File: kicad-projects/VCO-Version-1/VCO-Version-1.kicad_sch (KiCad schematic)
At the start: 41 parts

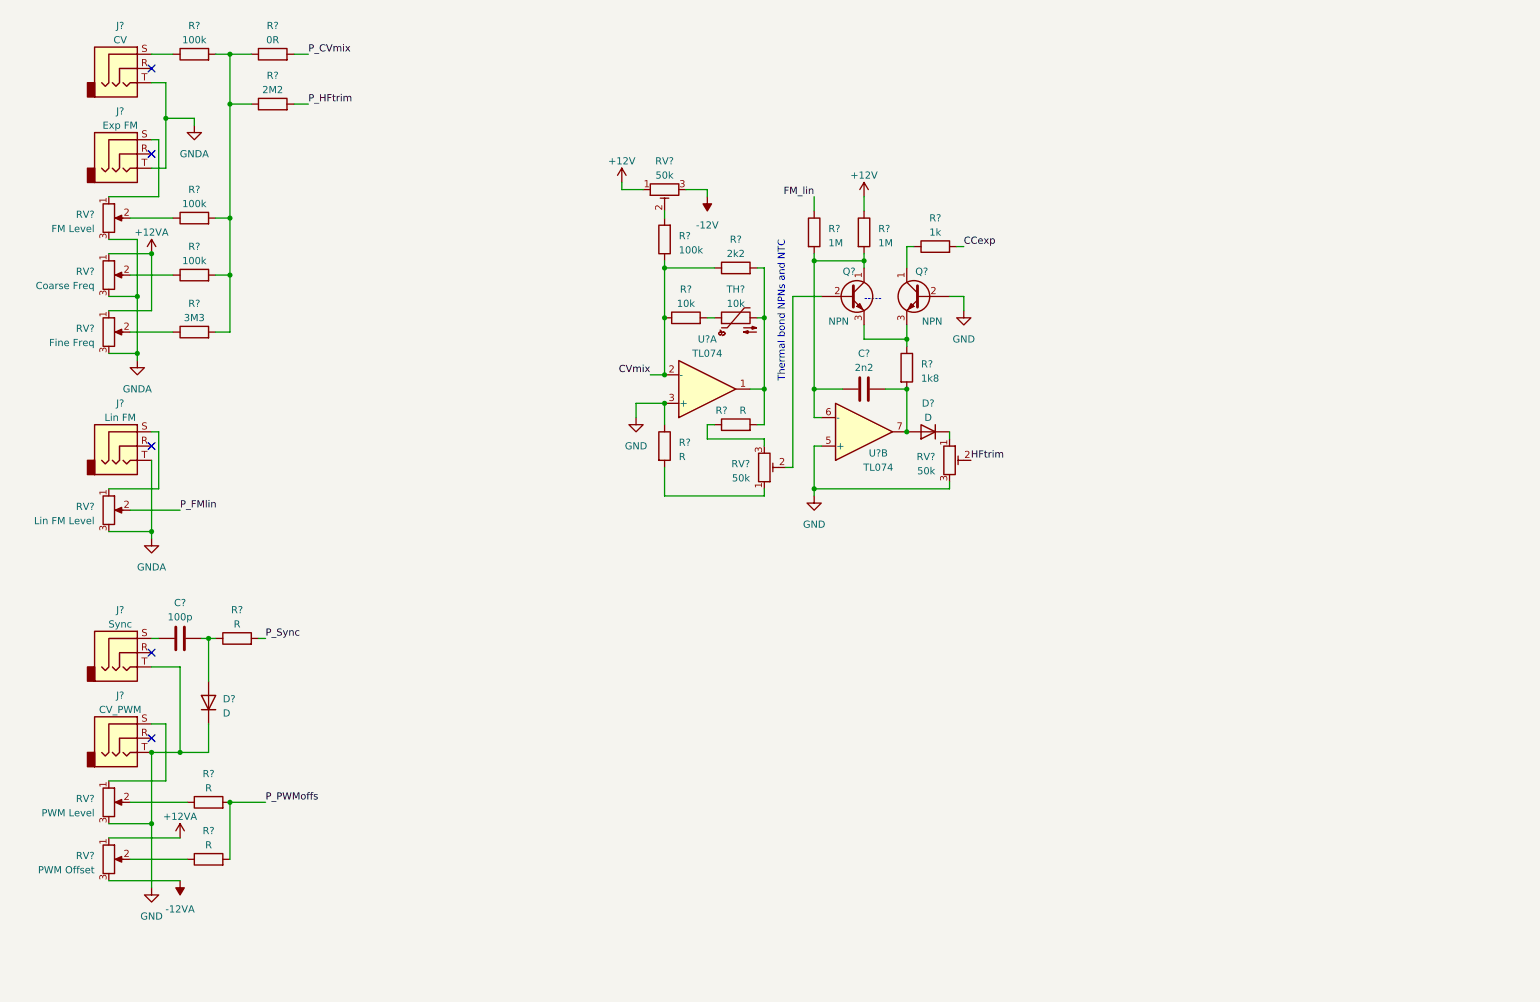
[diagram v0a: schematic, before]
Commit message: Completed schematic for VCO-1
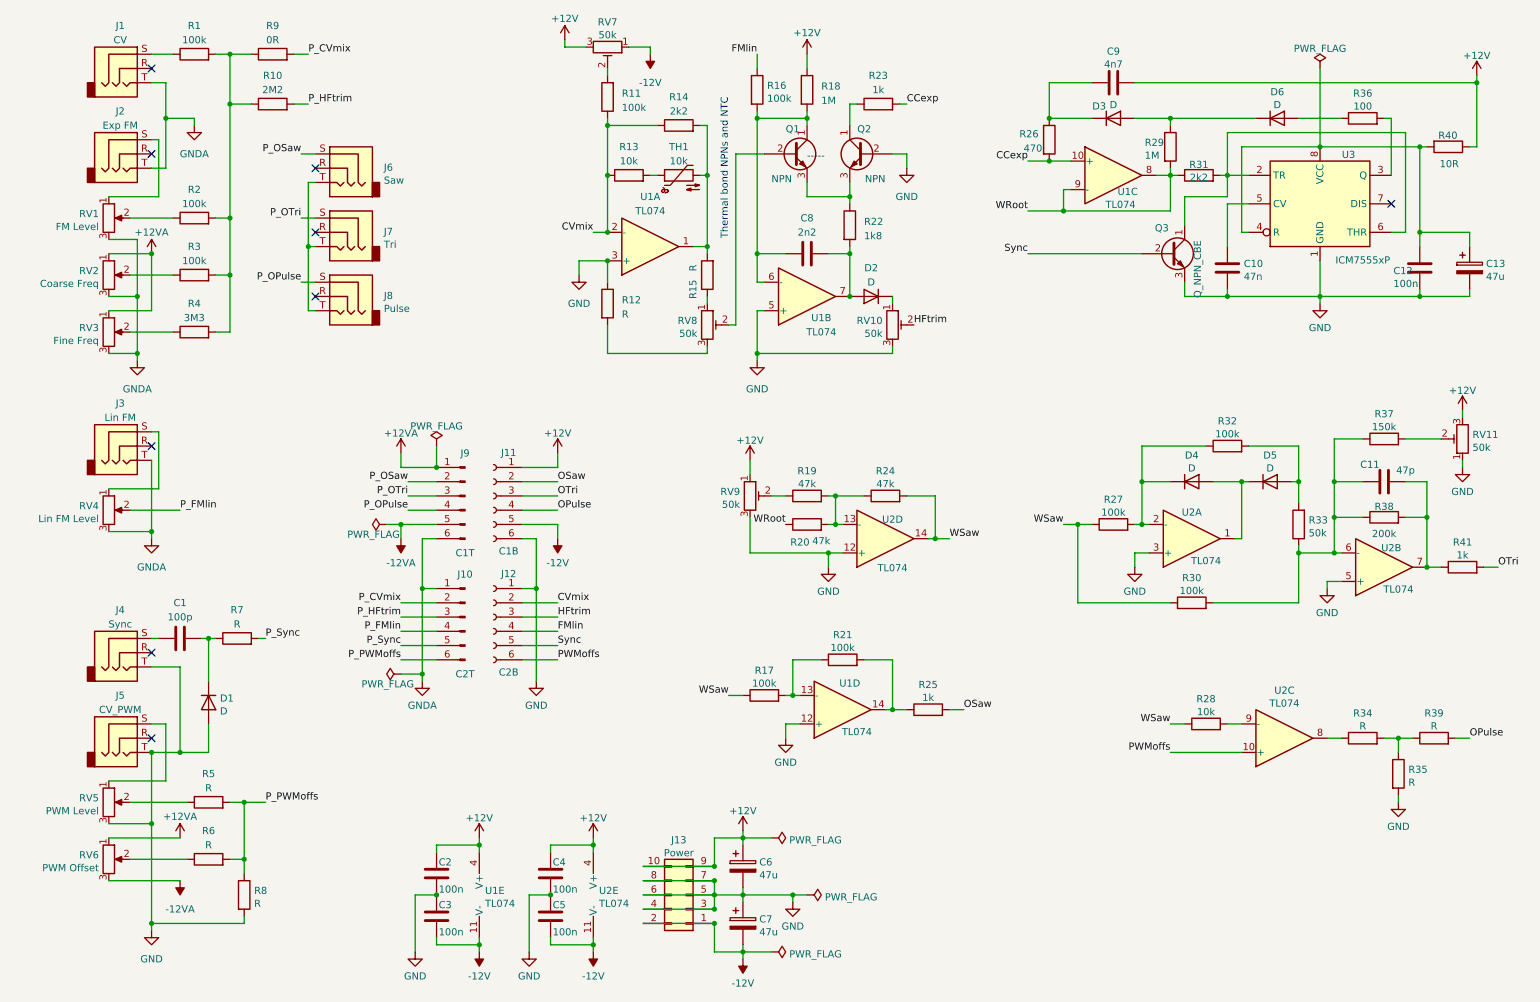
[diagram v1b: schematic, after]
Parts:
- removed RV?: FM Level, symbol Device:R_Potentiometer
- removed RV?: Lin FM Level, symbol Device:R_Potentiometer
- removed RV? (x3): 50k, symbol Device:R_Potentiometer_Trim
- removed RV?: PWM Offset, symbol Device:R_Potentiometer
- removed RV?: Fine Freq, symbol Device:R_Potentiometer
- removed RV?: Coarse Freq, symbol Device:R_Potentiometer
- removed RV?: PWM Level, symbol Device:R_Potentiometer
- added C10: 47n, symbol Device:C
- added C11: 47p, symbol Device:C
- added C12, C2, C3, C4, C5: 100n, symbol Device:C
- added C13, C6, C7: 47u, symbol Device:CP
- added C9: 4n7, symbol Device:C
- added D3, D4, D5, D6: D, symbol Device:D
- added J10: C2T, symbol Connector:Conn_01x06_Male
- added J11: C1B, symbol Connector:Conn_01x06_Female
- added J12: C2B, symbol Connector:Conn_01x06_Female
- added J13: Power, symbol Connector_Generic:Conn_02x05_Odd_Even
- added J6: Saw, symbol Connector:AudioJack3
- added J7: Tri, symbol Connector:AudioJack3
- added J8: Pulse, symbol Connector:AudioJack3
- added J9: C1T, symbol Connector:Conn_01x06_Male
- added Q3: Q_NPN_CBE, symbol Device:Q_NPN_CBE
- added R17, R21, R27, R30, R32: 100k, symbol Device:R
- added R19, R20, R24: 47k, symbol Device:R
- added R25, R41: 1k, symbol Device:R
- added R26: 470, symbol Device:R
- added R28: 10k, symbol Device:R
- added R29: 1M, symbol Device:R
- added R31: 2k2, symbol Device:R
- added R33: 50k, symbol Device:R
- added R34, R35, R39, R8: R, symbol Device:R
- added R36: 100, symbol Device:R
- added R37: 150k, symbol Device:R
- added R38: 200k, symbol Device:R
- added R40: 10R, symbol Device:R
- added RV1: FM Level, symbol Device:R_POT
- added RV10, RV11, RV7, RV8, RV9: 50k, symbol Device:R_POT_TRIM
- added RV2: Coarse Freq, symbol Device:R_POT
- added RV3: Fine Freq, symbol Device:R_POT
- added RV4: Lin FM Level, symbol Device:R_POT
- added RV5: PWM Level, symbol Device:R_POT
- added RV6: PWM Offset, symbol Device:R_POT
- added unit 3 of U1
- added unit 5 of U1
- added unit 4 of U1
- added U2: TL074, symbol Amplifier_Operational:TL074
- added U3: ICM7555xP, Package_DIP:DIP-8_W7.62mm, symbol Timer:ICM7555xP
- R16: renamed from R?; value 1M -> 100k
- gave numbers to parts that had none: 30
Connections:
- net +12V: now also C2.1, C4.1, C6.1, C9.2, J11.1 (Pin_1), J13.10 (Pin_10), J13.9 (Pin_9), R40.1, RV11.3, RV7.3, RV9.1, U1.4 (V+), U2.4 (V+)
- net +12VA: now also J9.1 (Pin_1), RV2.1, RV3.1, RV6.1
- net -12V: now also C3.2, C5.2, C7.2, J11.5 (Pin_5), J13.1 (Pin_1), J13.2 (Pin_2), RV7.1, U1.11 (V-), U2.11 (V-)
- net -12VA: now also J9.5 (Pin_5), RV6.3
- net CCexp: now also R26.2, U1.10 (+)
- net CVmix: now also J12.2 (Pin_2)
- net GND: now also D1.2 (A), C10.2, C12.2, C13.2, C2.2, C3.1, C4.2, C5.1, C6.2, C7.1, J11.6 (Pin_6), J12.1 (Pin_1), J13.3 (Pin_3), J13.4 (Pin_4), J13.5 (Pin_5), J13.6 (Pin_6), J13.7 (Pin_7), J13.8 (Pin_8), Q3.3 (E), R35.2, R8.2, RV10.3, RV11.1, RV5.3, RV9.3, U1.12 (+), U2.12 (+), U2.3 (+), U2.5 (+), U3.1 (GND); no longer D1.1 (K)
- net GNDA: now also J10.1 (Pin_1), J9.6 (Pin_6), RV1.3, RV2.3, RV3.3, RV4.3
- net HFtrim: now also J12.3 (Pin_3), RV10.2
- net P_CVmix: now also J10.2 (Pin_2)
- net P_FMlin: now also J10.4 (Pin_4), RV4.2
- net P_HFtrim: now also J10.3 (Pin_3)
- net P_PWMoffs: now also J10.6 (Pin_6), R8.1
- net P_Sync: now also J10.5 (Pin_5)
- net at J2.S: now also RV1.1
- net at R2.1: now also RV1.2
- net at R12.2: now also RV8.3
- net at Q1.2 (B): now also RV8.2
- net at J5.S: now also RV5.1
- net at J3.S: now also RV4.1
- net at R15.1: now also RV8.1
- net at R6.1: now also RV6.2
- net at C1.2, R7.1: now also D1.1 (K); no longer D1.2 (A)
- net at D2.1 (K): now also RV10.1
- net at R3.1: now also RV2.2
- net at R4.1: now also RV3.2
- net at R11.2: now also RV7.2
- net at R5.1: now also RV5.2
- net FM_lin renamed FMlin
- net FMlin: now also J12.4 (Pin_4)
- new net: C11.1, R30.2, R33.1, R37.1, R38.1, U2.6 (-)
- new net: C11.2, R38.2, R41.1, U2.7
- new net: R28.2, U2.9 (-)
- new net: R19.2, R20.2, R24.1, U2.13 (-)
- new net: D4.2 (A), D5.1 (K), U2.1
- new net: D4.1 (K), R27.2, R32.1, U2.2 (-)
- new net: C9.1, D3.1 (K), R26.1
- new net: C10.1, U3.5 (CV)
- new net: C12.1, C13.1, R40.2, U3.4 (R), U3.8 (VCC)
- new net: R34.2, R35.1, R39.1
- new net: R19.1, RV9.2
- new net: R17.2, R21.1, U1.13 (-)
- new net: Q3.1 (C), R31.2, U3.2 (TR), U3.6 (THR)
- new net: R36.2, U3.3 (Q)
- new net: J6.T, J7.T, J8.T
- new net: R34.1, U2.8
- new net: D5.2 (A), R32.2, R33.2
- new net: D3.2 (A), D6.1 (K), R29.1
- new net: D6.2 (A), R36.1
- new net: R21.2, R25.1, U1.14
- new net: R37.2, RV11.2
- new net OPulse: J11.4 (Pin_4), R39.2
- new net OSaw: J11.2 (Pin_2), R25.2
- new net OTri: J11.3 (Pin_3), R41.2
- new net PWMoffs: J12.6 (Pin_6), U2.10 (+)
- new net P_OPulse: J8.S, J9.4 (Pin_4)
- new net P_OSaw: J6.S, J9.2 (Pin_2)
- new net P_OTri: J7.S, J9.3 (Pin_3)
- new net Sync: J12.5 (Pin_5), Q3.2 (B)
- new net WRoot: R20.1, R29.2, R31.1, U1.8, U1.9 (-)
- new net WSaw: R17.1, R24.2, R27.1, R28.1, R30.1, U2.14
- no-connect marks 5 -> 9
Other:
- title: 40106 based VCO -> Three Wave VCO - v1
- moved on the sheet: C8, D1, D2, Q1, Q2, R11, R12, R13, R14, R15, R16, R18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

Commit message: Worked more on VCO1 PCB
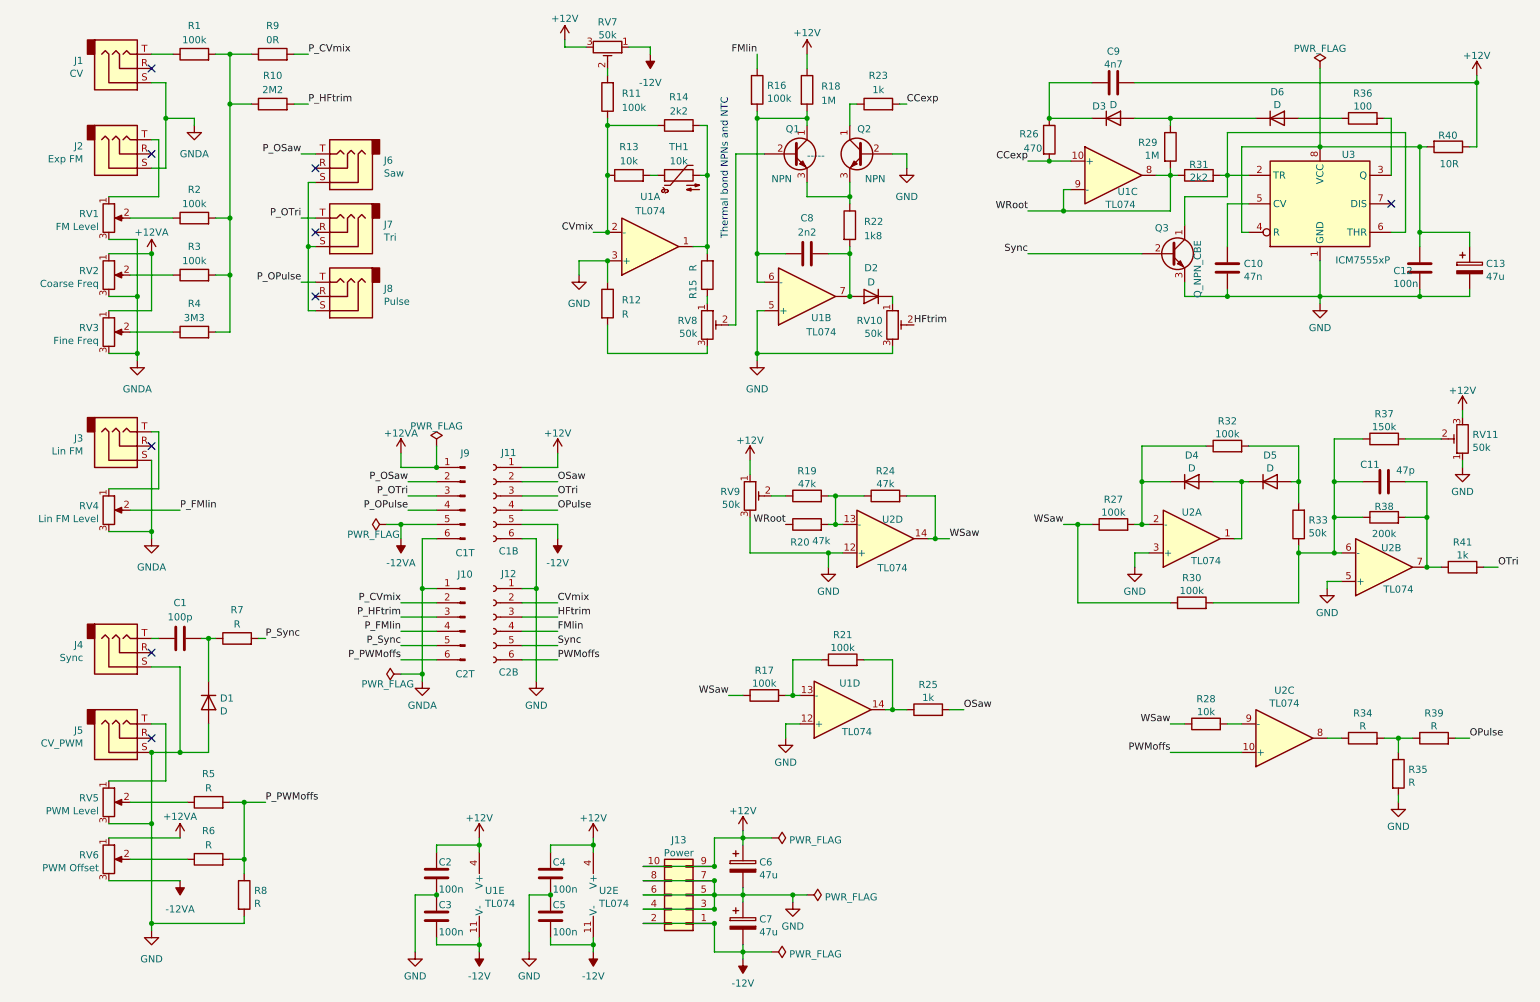
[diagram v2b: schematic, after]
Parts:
- C1, C10, C11, C12, C2, C3, C4, C5, C8, C9: footprint (none) -> Capacitor_THT:C_Rect_L7.0mm_W3.5mm_P5.00mm
- C13, C6, C7: footprint (none) -> Capacitor_THT:CP_Radial_D6.3mm_P2.50mm
- D1, D2, D3, D4, D5, D6: footprint (none) -> Diode_THT:D_DO-35_SOD27_P7.62mm_Horizontal
- J1, J2, J3, J4, J5, J6, J7, J8: footprint (none) -> Connector_Audio:Jack_3.5mm_QingPu_WQP-PJ398SM_Vertical_CircularHoles
- J10, J9: footprint (none) -> Connector_PinHeader_2.54mm:PinHeader_1x06_P2.54mm_Vertical
- J11, J12: footprint (none) -> Connector_PinSocket_2.54mm:PinSocket_1x06_P2.54mm_Vertical
- J13: footprint (none) -> Connector_IDC:IDC-Header_2x05_P2.54mm_Vertical
- Q1, Q2, Q3: footprint (none) -> Package_TO_SOT_THT:TO-92_Inline
- R1, R10, R11, R12, R13, R14, R15, R16, R17, R18, R19, R2, R20, R21, R22, R23, R24, R25, R26, R27, R28, R29, R3, R30, R31, R32, R33, R34, R35, R36, R37, R38, R39, R4, R40, R41, R5, R6, R7, R8, R9: footprint (none) -> Resistor_THT:R_Axial_DIN0207_L6.3mm_D2.5mm_P7.62mm_Horizontal
- RV1, RV2, RV3, RV4, RV5, RV6: footprint (none) -> Potentiometer_THT:Potentiometer_Alpha_RD901F-40-00D_Single_Vertical
- RV10, RV11, RV7, RV8, RV9: footprint (none) -> Potentiometer_THT:Potentiometer_Bourns_3296W_Vertical
- TH1: footprint (none) -> Resistor_THT:R_Axial_DIN0207_L6.3mm_D2.5mm_P2.54mm_Vertical
- U1, U2: footprint (none) -> Package_DIP:DIP-14_W7.62mm_Socket
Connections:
- net GND: now also J4.S, J5.S; no longer J4.T, J5.T
- net GNDA: now also J1.S, J2.S, J3.S; no longer J1.T, J2.T, J3.T
- net P_OPulse: now also J8.T; no longer J8.S
- net P_OSaw: now also J6.T; no longer J6.S
- net P_OTri: now also J7.T; no longer J7.S
- net at C1.1: now also J4.T; no longer J4.S
- net at R1.1: now also J1.T; no longer J1.S
- net at RV5.1: now also J5.T; no longer J5.S
- net at RV1.1: now also J2.T; no longer J2.S
- net at RV4.1: now also J3.T; no longer J3.S
- new net: J6.S, J7.S, J8.S
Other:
- moved on the sheet: J1, J2, J3, J4, J5, J6, J7, J8

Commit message: Added completed PCB layout which will likely be ordered.
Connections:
- net +12V: now also J11.4 (Pin_4); no longer J11.1 (Pin_1)
- net +12VA: now also J9.4 (Pin_4); no longer J9.1 (Pin_1)
- net -12V: now also J11.6 (Pin_6); no longer J11.5 (Pin_5)
- net -12VA: now also J9.6 (Pin_6); no longer J9.5 (Pin_5)
- net FMlin: now also J12.1 (Pin_1); no longer J12.4 (Pin_4)
- net GND: now also J11.5 (Pin_5), J12.5 (Pin_5); no longer D1.2 (A), J11.6 (Pin_6), J12.1 (Pin_1), J4.S, J5.S, R8.2, RV5.3
- net GNDA: now also D1.2 (A), J10.5 (Pin_5), J4.S, J5.S, J6.S, J7.S, J8.S, J9.5 (Pin_5), R8.2, RV5.3; no longer J10.1 (Pin_1), J9.6 (Pin_6)
- net HFtrim: now also J11.1 (Pin_1); no longer J12.3 (Pin_3)
- net OPulse: now also J12.4 (Pin_4); no longer J11.4 (Pin_4)
- net OSaw: now also J12.3 (Pin_3); no longer J11.2 (Pin_2)
- net OTri: now also J12.6 (Pin_6); no longer J11.3 (Pin_3)
- net PWMoffs: now also J11.3 (Pin_3); no longer J12.6 (Pin_6)
- net P_FMlin: now also J10.1 (Pin_1); no longer J10.4 (Pin_4)
- net P_HFtrim: now also J9.1 (Pin_1); no longer J10.3 (Pin_3)
- net P_OPulse: now also J10.4 (Pin_4); no longer J9.4 (Pin_4)
- net P_OSaw: now also J10.3 (Pin_3); no longer J9.2 (Pin_2)
- net P_OTri: now also J10.6 (Pin_6); no longer J9.3 (Pin_3)
- net P_PWMoffs: now also J9.3 (Pin_3); no longer J10.6 (Pin_6)
- net P_Sync: now also J9.2 (Pin_2); no longer J10.5 (Pin_5)
- net Sync: now also J11.2 (Pin_2); no longer J12.5 (Pin_5)
